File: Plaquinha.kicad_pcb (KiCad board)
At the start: 2 copper layers, 32 parts, among them J1 Screw_Terminal_01x02, J10 Conn_01x15_Socket, J11 Conn_01x15_Socket, J12 Conn_01x06_Socket, J2 Conn_01x10_Socket, J3 Conn_01x10_Socket, J4 Conn_01x06_Socket, J5 Conn_01x04_Socket, J6 Conn_01x04_Socket, J8 Conn_01x03_Socket, J9 Conn_01x03_Socket, U1 L7805, U10 TA6586, U3 TA6586, U5 L7805, U9 ESP32-DEVKIT-V1

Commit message: PCB e Sketch atualizados
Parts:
- added ?: , , F.Cu at (110.0, 66.2)
- added ?: , , F.Cu at (122.1, 58.8)
- added ?: , , F.Cu at (128.8, 73.6)
- added ?: , , F.Cu at (123.8, 61.4)
- added ?: , , F.Cu at (152.9, 88.6)
- added ?: , , F.Cu at (153.0, 83.0)
- added ?: , , F.Cu at (128.8, 56.8)
- added J13: Conn_01x06_Socket, Connector_PinHeader_2.54mm:PinHeader_1x06_P2.54mm_Vertical, F.Cu at (72.0, 100.1)
- added J7: Conn_01x06_Socket, Connector_PinHeader_2.54mm:PinHeader_1x06_P2.54mm_Vertical, F.Cu at (54.5, 100.1)
- C1: footprint Capacitor_THT:C_Disc_D5.0mm_W2.5mm_P5.00mm -> Capacitor_THT:C_Disc_D5.0mm_W2.5mm_P2.50mm
- moved C9 77.6 mm to (137.0, 53.9), turned to 0 degrees
- moved D3 68.3 mm to (134.6, 46.0), turned to 180 degrees
- moved R3 67.2 mm to (132.1, 54.3)
- moved J5 36.0 mm to (105.5, 85.5)
- moved J6 36.0 mm to (105.5, 78.5)
- moved J8 35.6 mm to (90.6, 85.8)
- moved J9 35.6 mm to (90.6, 78.8)
- moved BZ1 30.9 mm to (79.2, 80.2), turned to 180 degrees
- moved C3 26.4 mm to (143.9, 85.8), turned to 0 degrees
- moved D1 23.1 mm to (155.6, 56.3), turned to 180 degrees
- moved C2 22.4 mm to (156.1, 86.6), turned to 0 degrees
- moved C5 20.2 mm to (151.5, 92.4), turned to 180 degrees
- moved C1 18.8 mm to (142.2, 106.5), turned to 0 degrees
- moved C6 18.3 mm to (157.8, 106.4), turned to 0 degrees
- moved J3 18.0 mm to (93.5, 114.1), turned to 90 degrees
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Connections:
- C1 pad 1: (no net) -> OUTMOT1
- C1 pad 2: (no net) -> OUTMOT2
- J10 pad 11: D21 -> SDA
- J10 pad 14: D22 -> SCL
- J10 pad 6: RX2 -> unconnected-(J10-Pin_6-Pad6)
- J10 pad 7: TX2 -> unconnected-(J10-Pin_7-Pad7)
- J11 pad 7: D26 -> TRIG
- J11 pad 8: D25 -> ECHO
- J6 pad 2: TRIG -> TRIG5V
- J6 pad 3: ECHO -> ECHO5V
- U9 pad 23: unconnected-(U9-D25-Pad23) -> ECHO
- U9 pad 24: unconnected-(U9-D26-Pad24) -> TRIG
- U9 pad 25: encode2 A -> encode2 B
- U9 pad 26: encode2 B -> encode2 A
- U9 pad 6: ECHO -> unconnected-(U9-RX2-Pad6)
- U9 pad 7: TRIG -> unconnected-(U9-TX2-Pad7)
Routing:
- net IN3: track 3.72 -> 93.1 mm
- net IN4: track 3.00 -> 89.5 mm
- net IN2: track 4.20 -> 80.2 mm
- net IN1: track 6.13 -> 78.7 mm
- net GND: track 273.8 -> 343.8 mm
- net +5V: track 123.0 -> 168.7 mm
- net 3.3V: track 87.8 -> 131.8 mm
- net Net-(D1-K): track 54.2 -> 23.7 mm
- net encode1 A: track 137.3 -> 113.4 mm
- net D33: track 3.60 -> 26.7 mm
- net encode1 B: track 140.2 -> 119.0 mm
- net OUTMOT1: track 33.8 -> 18.6 mm
- net OUTMOT4: track 26.0 -> 14.0 mm
- net encode2 B: track 64.3 -> 59.0 mm
- net encode2 A: track 66.9 -> 61.6 mm
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
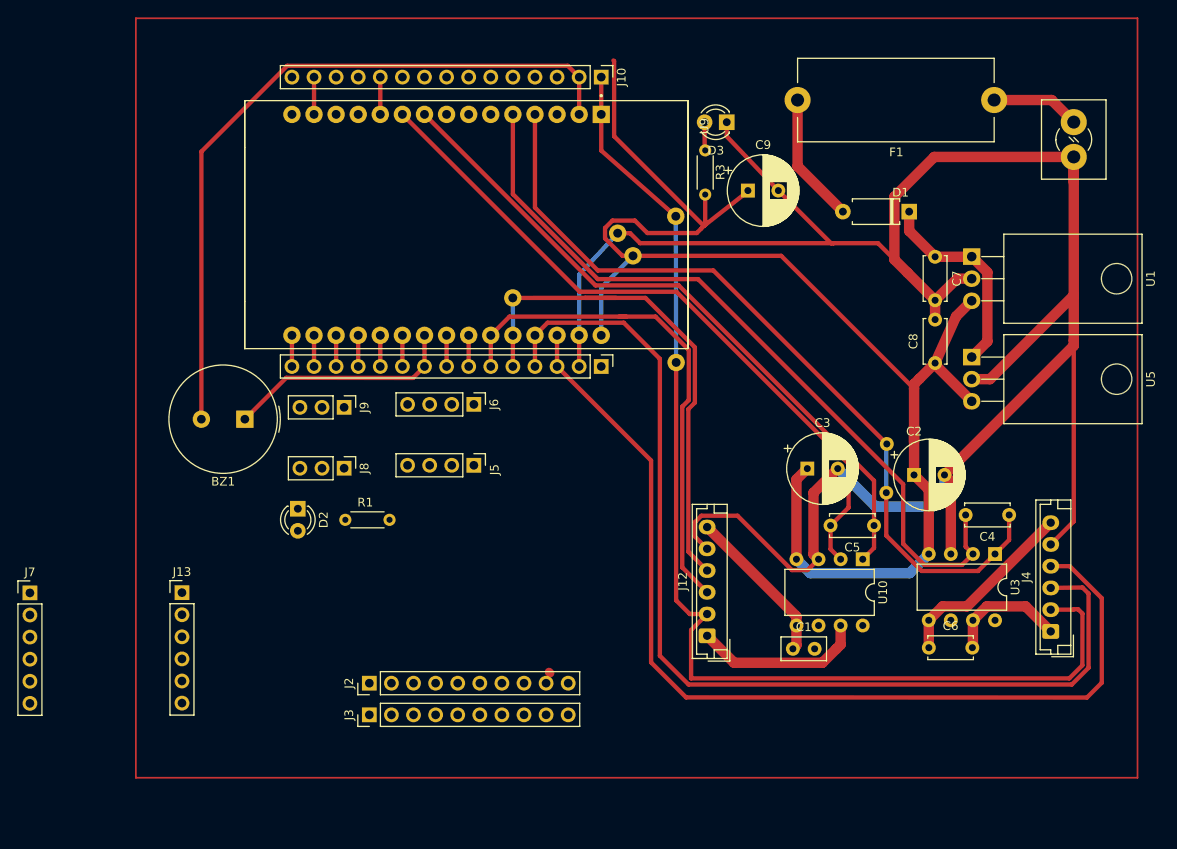
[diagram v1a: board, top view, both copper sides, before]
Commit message: PCI finalizada e shunt jumper adicionado ao sketch
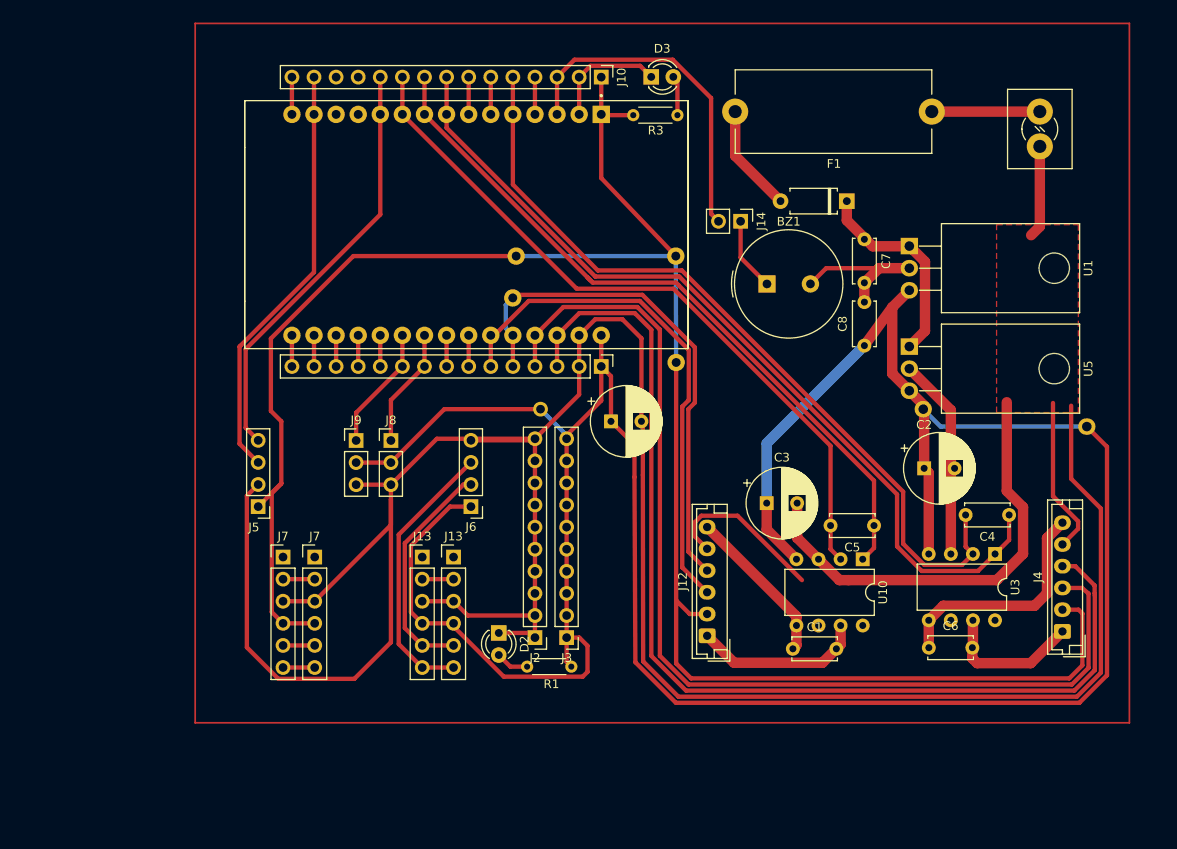
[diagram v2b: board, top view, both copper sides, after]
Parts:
- removed the ? at (122.1, 58.8)
- removed the ? at (123.8, 61.4)
- removed the ? at (152.9, 88.6)
- removed the ? at (153.0, 83.0)
- added ?: , , F.Cu at (110.4, 61.4)
- added ?: , , F.Cu at (113.2, 79.0)
- added ?: , , F.Cu at (176.0, 81.0)
- added ?: , , F.Cu at (157.2, 79.0)
- added J13: Conn_01x06_Socket, Connector_PinHeader_2.54mm:PinHeader_1x06_P2.54mm_Vertical, F.Cu at (103.2, 96.0)
- added J14: Conn_01x06_Socket, Connector_PinHeader_2.54mm:PinHeader_1x02_P2.54mm_Vertical, F.Cu at (136.2, 57.4)
- added J7: Conn_01x06_Socket, Connector_PinHeader_2.54mm:PinHeader_1x06_P2.54mm_Vertical, F.Cu at (83.6, 96.0)
- C1: footprint Capacitor_THT:C_Disc_D5.0mm_W2.5mm_P2.50mm -> Capacitor_THT:C_Disc_D5.0mm_W2.5mm_P5.00mm
- moved BZ1 62.0 mm to (139.2, 64.6), turned to 0 degrees
- moved J7 33.0 mm to (87.2, 96.0)
- moved R1 31.0 mm to (116.7, 108.6), turned to 180 degrees
- moved C9 30.8 mm to (121.3, 80.4)
- moved J13 27.9 mm to (99.6, 96.0)
- moved D2 27.2 mm to (108.4, 104.7)
- moved J5 25.2 mm to (80.7, 90.2), turned to 180 degrees
- moved J3 24.4 mm to (116.2, 105.3), turned to 180 degrees
- moved J2 19.7 mm to (112.6, 105.3), turned to 180 degrees
- moved R3 12.3 mm to (123.9, 45.2), turned to 0 degrees
- moved J6 11.8 mm to (105.2, 90.2), turned to 180 degrees
- moved D3 10.1 mm to (125.9, 40.8), turned to 0 degrees
- moved C7 8.38 mm to (150.4, 59.5)
- moved C8 8.38 mm to (150.4, 71.7)
- moved F1 7.29 mm to (158.2, 44.8)
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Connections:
- BZ1 pad 1: D33 -> BUZZER
- J10 pad 1: 3.3v -> 3.3V
- J10 pad 10: D19 -> IN2
- J10 pad 3: D15 -> BUZZER
- J10 pad 5: D4 -> IN4
- J10 pad 6: unconnected-(J10-Pin_6-Pad6) -> RX2
- J10 pad 7: unconnected-(J10-Pin_7-Pad7) -> TX2
- J10 pad 8: D5 -> IN3
- J10 pad 9: D18 -> IN1
- J11 pad 10: D32 -> sinal2
- J11 pad 9: D33 -> sinal1
- R3 pad 1: +5V -> unconnected-(R3-Pad1)
- U9 pad 15: sinal1 -> D23
- U9 pad 21: D32 -> sinal2
- U9 pad 22: D33 -> sinal1
- U9 pad 3: sinal2 -> BUZZER
- U9 pad 4: IN3 -> D2
- U9 pad 6: unconnected-(U9-RX2-Pad6) -> RX2
- U9 pad 7: unconnected-(U9-TX2-Pad7) -> TX2
- U9 pad 8: unconnected-(U9-D5-Pad8) -> IN3
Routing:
- net +5V: track 168.7 -> 326.4 mm
- net GND: track 343.8 -> 447.8 mm
- net 3.3V: track 131.8 -> 227.4 mm
- net BUZZER: track 0.00 -> 47.6 mm
- net SDA: track 4.28 -> 48.8 mm
- net SCL: track 4.28 -> 48.7 mm
- net ECHO5V: track 0.00 -> 31.7 mm
- net D33: track 26.7 -> 0.00 mm
- net TRIG5V: track 0.00 -> 26.6 mm
- net sinal2: track 0.00 -> 14.3 mm
- net sinal1: track 0.00 -> 13.7 mm
- net encode1 A: track 113.4 -> 121.7 mm
- net IN3: track 93.1 -> 99.5 mm
- net OUTMOT3: track 21.8 -> 26.9 mm
- net IN1: track 78.7 -> 83.5 mm
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- added copper zone on F.Cu, net GND

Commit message: Atualizei PCI, tirei jumpers desnecessários e simplifiquei trilhas
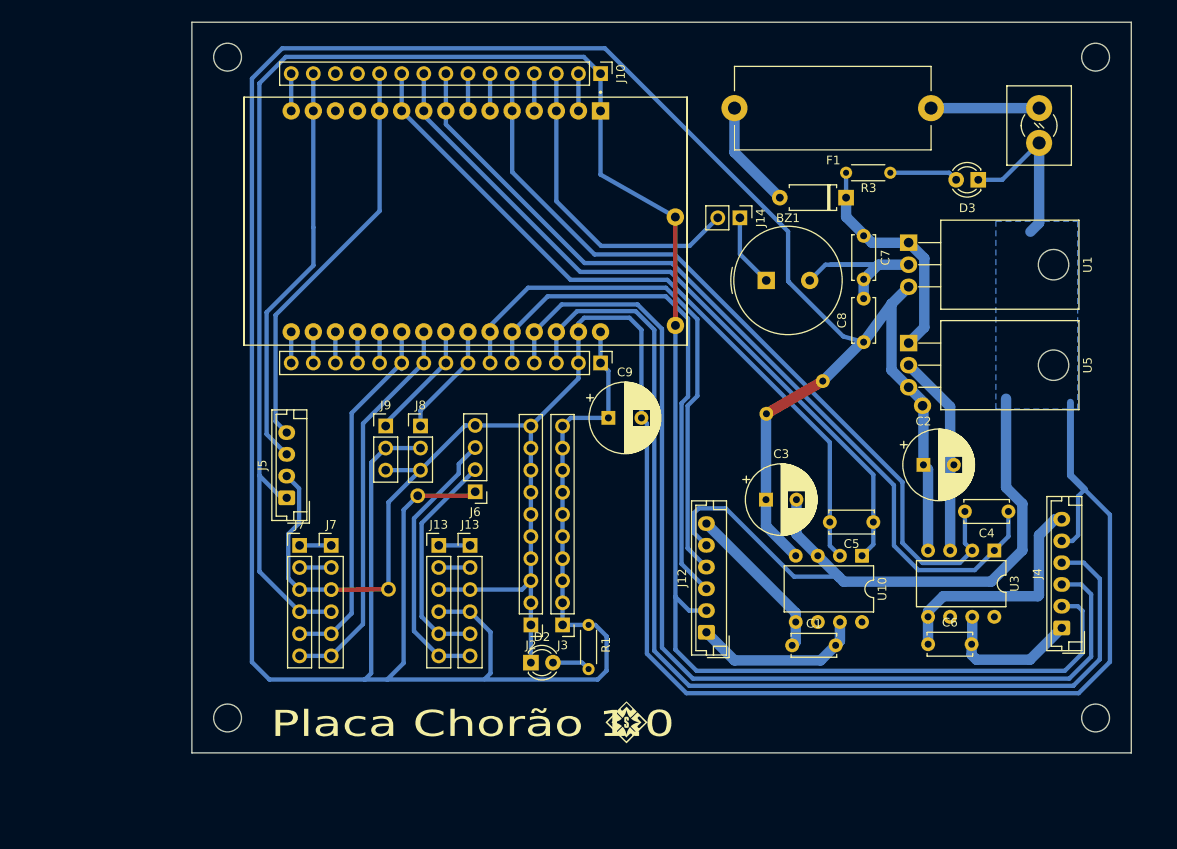
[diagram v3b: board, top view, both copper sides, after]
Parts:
- removed the ? at (110.4, 61.4)
- removed the ? at (110.0, 66.2)
- removed the ? at (176.0, 81.0)
- added ?: , , F.Cu at (145.6, 75.8)
- added ?: , , F.Cu at (139.2, 79.5)
- added ?: , , F.Cu at (95.7, 99.7)
- added REF**: MountingHole_3.2mm_M3, MountingHole:MountingHole_3.2mm_M3, F.Cu at (77.2, 114.5)
- added REF**: MountingHole_3.2mm_M3, MountingHole:MountingHole_3.2mm_M3, F.Cu at (77.2, 38.5)
- added REF**: MountingHole_3.2mm_M3, MountingHole:MountingHole_3.2mm_M3, F.Cu at (177.0, 114.5)
- added REF**: MountingHole_3.2mm_M3, MountingHole:MountingHole_3.2mm_M3, F.Cu at (177.0, 38.5)
- C9: footprint Capacitor_THT:CP_Radial_D8.0mm_P3.50mm -> Capacitor_THT:CP_Radial_D8.0mm_P3.80mm
- J5: footprint Connector_PinHeader_2.54mm:PinHeader_1x04_P2.54mm_Vertical -> Connector_JST:JST_EH_B4B-EH-A_1x04_P2.50mm_Vertical
- moved D3 39.4 mm to (163.5, 52.6), turned to 180 degrees
- moved R3 25.3 mm to (148.3, 51.8)
- moved ? 17.3 mm to (99.1, 89.0)
- moved R1 5.19 mm to (118.7, 103.8), turned to -90 degrees
- moved D2 5.03 mm to (112.1, 108.1), turned to 0 degrees
- moved ? 4.49 mm to (128.7, 56.9)
- moved ? 4.26 mm to (128.7, 69.4)
- moved J8 3.79 mm to (99.4, 80.9)
- moved J9 3.79 mm to (95.4, 80.9)
- moved J5 3.43 mm to (84.0, 89.2), turned to 90 degrees
- moved J13 2.32 mm to (101.5, 94.7)
- moved J7 2.32 mm to (85.5, 94.7)
- moved J7 2.32 mm to (89.1, 94.7)
- moved J13 2.32 mm to (105.1, 94.7)
- moved J6 1.78 mm to (105.7, 88.5)
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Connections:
- J11 pad 1: unconnected-(J11-Pin_1-Pad1) -> +5V
- J11 pad 10: sinal2 -> TRIG3V
- J11 pad 3: D13 -> encode1 A
- J11 pad 4: D12 -> encode1 B
- J11 pad 5: D14 -> encode2 B
- J11 pad 6: D27 -> encode2 A
- J11 pad 7: TRIG -> sinal1
- J11 pad 8: ECHO -> sinal2
- J11 pad 9: sinal1 -> ECHO3V
- J7 pad 6: unconnected-(J7-Pin_6-Pad6) -> ECHO3V (x2)
- R3 pad 1: unconnected-(R3-Pad1) -> Net-(D1-K)
- U9 pad 21: sinal2 -> TRIG3V
- U9 pad 22: sinal1 -> ECHO3V
- U9 pad 23: ECHO -> sinal2
- U9 pad 24: TRIG -> sinal1
- U9 pad 25: encode2 B -> encode2 A
- U9 pad 26: encode2 A -> encode2 B
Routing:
- net +5V: track 326.4 -> 391.2 mm
- net GND: track 447.8 -> 400.1 mm
- net ECHO3V: track 0.00 -> 44.6 mm
- net TRIG3V: track 3.64 -> 41.7 mm
- net 3.3V: track 227.4 -> 243.4 mm
- net unconnected-(J7-Pin_6-Pad6): track 3.64 -> 0.00 mm
- net unconnected-(J7-Pin_1-Pad1): track 0.00 -> 3.64 mm
- net unconnected-(J13-Pin_1-Pad1): track 0.00 -> 3.60 mm
- net TRIG: track 3.58 -> 0.00 mm
- net ECHO: track 3.58 -> 0.00 mm
- net Net-(D3-A): track 4.60 -> 7.91 mm
- net Net-(D1-K): track 23.7 -> 26.5 mm
- net BUZZER: track 47.6 -> 45.1 mm
- net SDA: track 48.8 -> 46.7 mm
- net encode2 A: track 59.0 -> 61.0 mm
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- added copper zone on B.Cu, net GND
- removed copper zone on F.Cu, net GND
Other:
- board outline added: 108 x 84 mm
- board text added: "Placa Chorão 1.0"

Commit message: Placa corrigida e pronta para impressão
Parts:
- renumbered J7 to J15, J13 to J16
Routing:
- net GND: track 400.1 -> 393.6 mm
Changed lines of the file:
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@@
 		(descr "Through hole straight pin header, 1x06, 2.54mm pitch, single row")
 		(tags "Through hole pin header THT 1x06 2.54mm single row")
-		(property "Reference" "J7"
+		(property "Reference" "J15"
 			(at 0 -2.38 0)
 			(layer "F.SilkS")
@@
 	(footprint "Package_TO_SOT_THT:TO-220-3_Horizontal_TabDown"
 		(layer "F.Cu")
-		(at 155.517678 71.401 -90)
+		(at 155.49 71.38 -90)
 		(descr "TO-220-3, Horizontal, RM 2.54mm, see https://www.vishay.com/docs/66542/to-220-1.pdf")
 		(tags "TO-220-3 Horizontal RM 2.54mm")
@@
 			)
 		)
-		(pad "" np_thru_hole oval
+		(pad "" thru_hole oval
 			(at 2.54 -16.66 270)
 			(size 3.5 3.5)
-			(drill 3.5)
+			(drill 3)
 			(layers "*.Cu" "*.Mask")
+			(remove_unused_layers no)
 		)
 		(pad "1" thru_hole rect
@@
 			)
 		)
-		(pad "" np_thru_hole oval
+		(pad "" thru_hole oval
 			(at 2.54 -16.66 270)
 			(size 3.5 3.5)
-			(drill 3.5)
+			(drill 3)
 			(layers "*.Cu" "*.Mask")
+			(remove_unused_layers no)
 		)
 		(pad "1" thru_hole rect
@@
 		(descr "Through hole straight pin header, 1x06, 2.54mm pitch, single row")
 		(tags "Through hole pin header THT 1x06 2.54mm single row")
-		(property "Reference" "J13"
+		(property "Reference" "J16"
 			(at 0 -2.38 0)
 			(layer "F.SilkS")
@@
 	)
 	(segment
-		(start 168.589678 89.871)
-		(end 168.589678 95.231)
-		(width 1.2)
-		(layer "B.Cu")
-		(net 1)
-	)
-	(segment
 		(start 175 89)
 		(end 175.759339 88.240661)
@@
 	)
 	(segment
-		(start 166.718678 77.8)
-		(end 166.718678 88)
-		(width 1.2)
-		(layer "B.Cu")
-		(net 1)
-	)
-	(segment
 		(start 152.027678 62.391)
 		(end 150.347678 64.071)
@@
 	)
 	(segment
-		(start 166.718678 88)
-		(end 168.589678 89.871)
+		(start 164.990678 98.83)
+		(end 148.058678 98.83)
 		(width 1.2)
 		(layer "B.Cu")
@@
 	)
 	(segment
+		(start 168.589678 78.299678)
+		(end 168.589678 95.231)
+		(width 1.2)
+		(layer "B.Cu")
+		(net 1)
+	)
+	(segment
 		(start 85.447322 88.116)
 		(end 84.021322 86.69)
@@
 	)
 	(segment
-		(start 148.058678 98.83)
-		(end 147.481677 98.252999)
-		(width 1.2)
-		(layer "B.Cu")
-		(net 1)
-	)
-	(segment
 		(start 163.52 52.63)
 		(end 166.279678 52.63)
@@
 	)
 	(segment
-		(start 101.5 99.74)
-		(end 105.1 99.74)
-		(width 0.5)
+		(start 160.718678 81.021322)
+		(end 163.73 78.01)
+		(width 1.2)
 		(layer "B.Cu")
 		(net 1)
 	)
 	(segment
-		(start 160.288678 85.83)
-		(end 160.718678 85.4)
+		(start 148.058678 98.83)
+		(end 147.481677 98.252999)
 		(width 1.2)
 		(layer "B.Cu")
@@
 	)
 	(segment
-		(start 164.990678 98.83)
-		(end 148.058678 98.83)
-		(width 1.2)
+		(start 101.5 99.74)
+		(end 105.1 99.74)
+		(width 0.5)
 		(layer "B.Cu")
 		(net 1)
 	)
 	(segment
-		(start 160.288678 78.712)
-		(end 155.517678 73.941)
+		(start 160.288678 85.83)
+		(end 160.718678 85.4)
 		(width 1.2)
 		(layer "B.Cu")
@@
 	)
 	(segment
-		(start 99.4 86.01)
-		(end 95.4 86.01)
-		(width 0.5)
+		(start 160.718678 85.4)
+		(end 160.718678 81.021322)
+		(width 1.2)
 		(layer "B.Cu")
 		(net 1)
 	)
 	(segment
-		(start 160.288678 85.83)
-		(end 160.288678 78.712)
-		(width 1.2)
+		(start 99.4 86.01)
+		(end 95.4 86.01)
+		(width 0.5)
 		(layer "B.Cu")
 		(net 1)
@@
 		(polygon
 			(pts
-				(xy 174.947678 57.391) (xy 174.947678 78.991) (xy 165.547678 78.991) (xy 165.547678 57.391)
+				(xy 174.947678 57.391) (xy 174.947678 78.991) (xy 161.867678 78.991) (xy 161.867678 57.391)
 			)
 		)
